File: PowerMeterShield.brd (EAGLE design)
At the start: 71.1 x 53.3 mm, 28 parts, among them IC1 MCP3426A0-E/SN, IC2 ISL21080, IC3 ADUM1250ARZ, U1 INA170EA/2K5, U2 THS4521

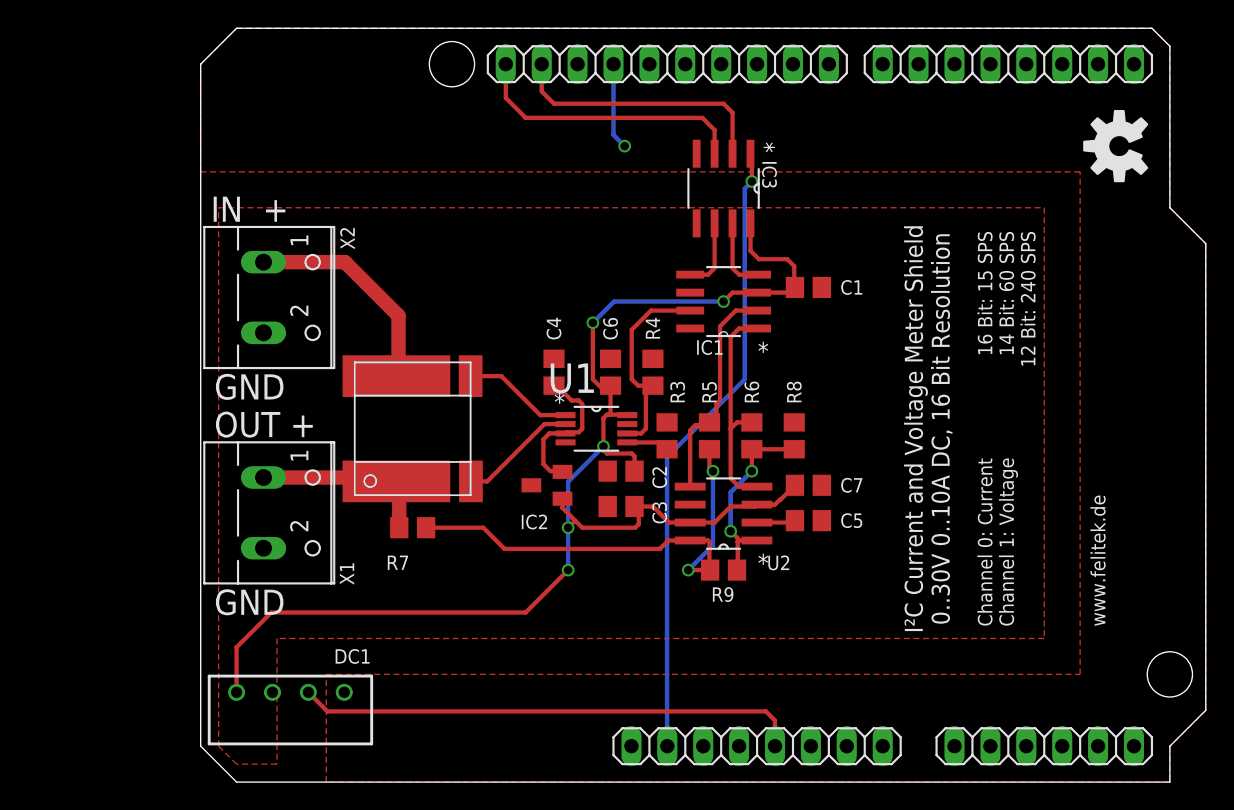
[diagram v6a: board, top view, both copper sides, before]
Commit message: Added non-isolated variant
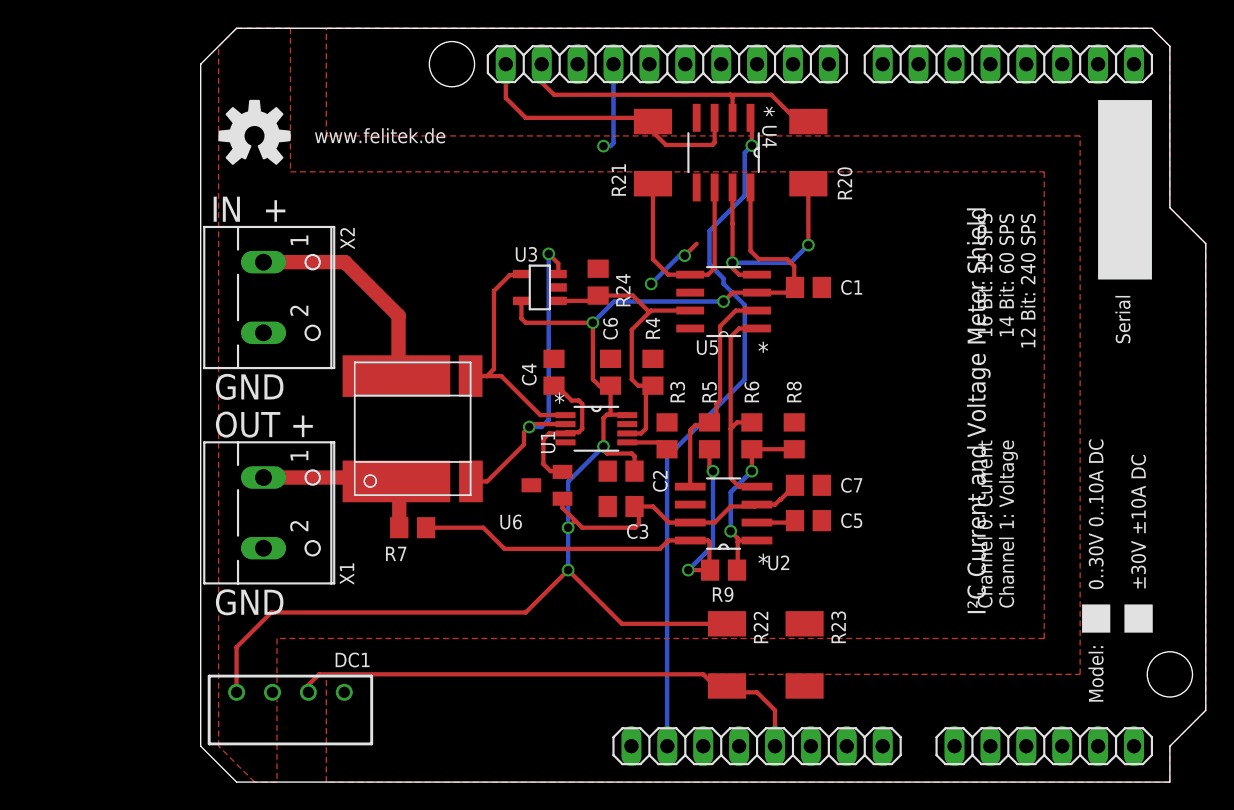
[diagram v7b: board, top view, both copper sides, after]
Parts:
- removed IC3: ADUM1250ARZ, Adum1250:SOIC127P600X175-8N
- added R20, R21, R22, R23: 0, rcl:R2010
- added R24: 20k, rcl:R0805
- added U3: INA138, burr-brown:SOT23-5
- added U4: ADUM1250ARZ, Adum1250:SOIC127P600X175-8N
- moved U$1 61.2 mm to (3.81, 45.7), turned to 0 degrees
- renumbered IC1 to U5, IC2 to U6, RS1 to R1
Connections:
- net +5V: now also R22.2
- net +5V/2: now also R22.1, U3.5, U4.8; no longer IC3.8
- net ADC2: now also R24.2, U3.1
- net CURRENT+: now also U3.3
- net CURRENT-: now also U3.4
- net GND: now also R23.2, U4.4; no longer IC3.4
- net GNDI: now also R23.1, R24.1, U3.2, U4.5; no longer IC3.5
- net IOREF: now also U4.1; no longer IC3.1
- net SCL: now also R21.2, U4.3; no longer IC3.3
- net SCLI: now also R21.1, U4.6; no longer IC3.6
- net SDA: now also R20.2, U4.2; no longer IC3.2
- net SDAI: now also R20.1, U4.7; no longer IC3.7
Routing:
- net +5V/2: track 97.9 -> 119.7 mm
- net CURRENT+: track 8.37 -> 23.9 mm, vias 0 -> 2
- net SDAI: track 5.09 -> 17.9 mm, vias 0 -> 2
- net SCLI: track 5.09 -> 16.1 mm
- net CURRENT-: track 7.86 -> 16.5 mm
- net ADC2: track 14.6 -> 21.7 mm
- net SDA: track 19.0 -> 24.1 mm
- net IOREF: track 44.5 -> 49.1 mm
- net GNDI: track 0.00 -> 4.56 mm, vias 0 -> 2
- net +5V: track 35.7 -> 38.1 mm
- net SCL: track 19.8 -> 21.1 mm
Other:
- board text added: "0..30V 0..10A DC"
- board text added: "I²C Current and Voltage Meter Shield"
- board text added: "Model:"
- board text added: "Serial"
- board text added: "±30V ±10A DC"
- board text removed: "I²C Current and Voltage Meter Shield 0..30V 0..10A DC, 16 Bit Resolution"

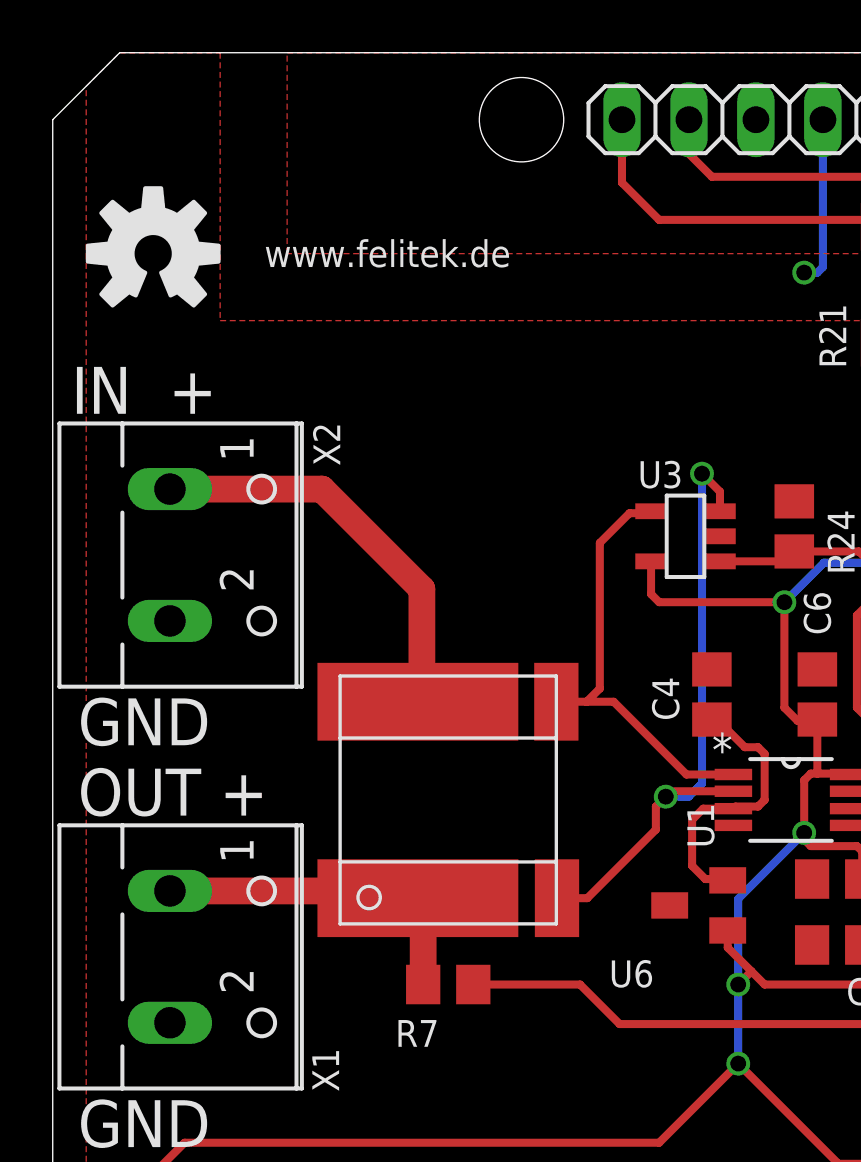
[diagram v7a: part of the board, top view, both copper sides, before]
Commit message: Moved logo and website a bit towards the top to align nicely with the isolation
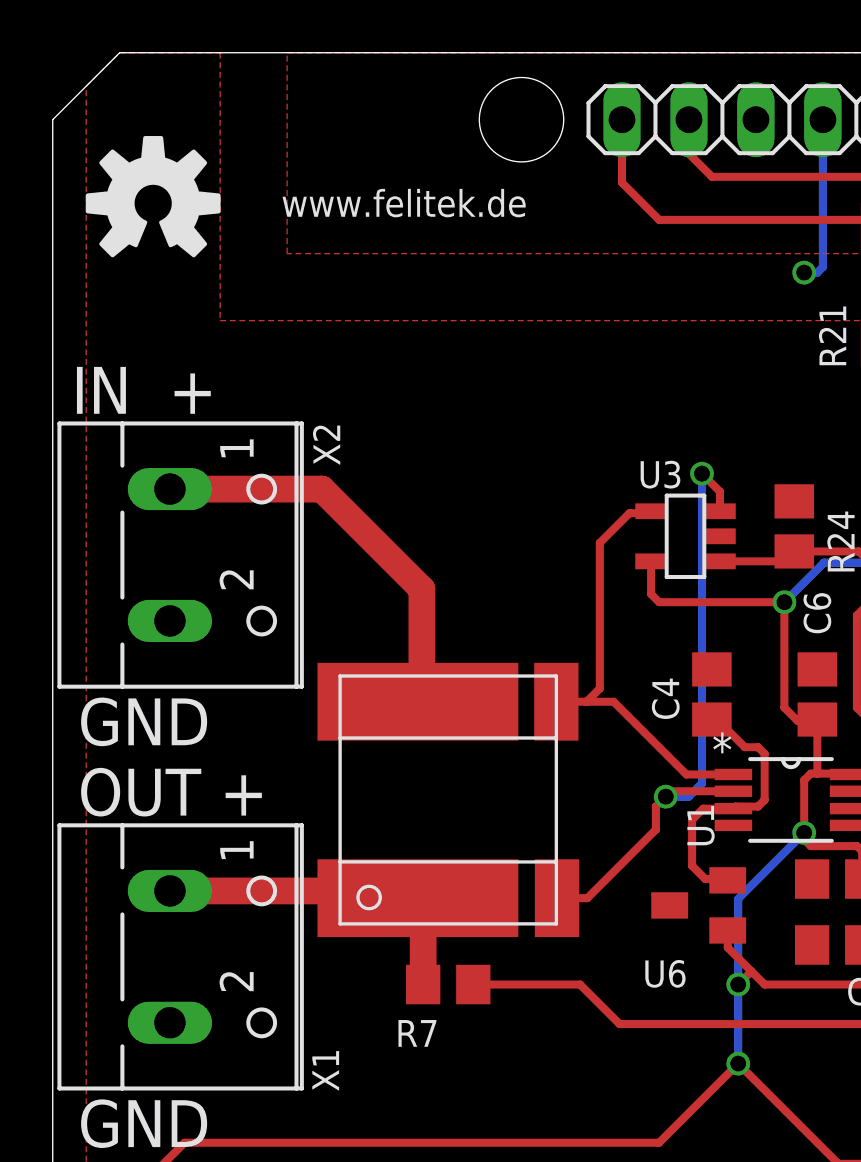
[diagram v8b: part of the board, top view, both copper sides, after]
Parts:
- moved U$1 1.91 mm to (3.81, 47.6)
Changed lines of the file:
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@@
 <rectangle x1="62.365" y1="10.57" x2="64.365" y2="12.57" layer="25"/>
 <rectangle x1="65.365" y1="10.57" x2="67.365" y2="12.57" layer="25"/>
-<text x="12.7" y="45.72" size="1.016" layer="25" align="center">www.felitek.de</text>
+<text x="13.335" y="47.625" size="1.016" layer="25" align="center">www.felitek.de</text>
 <rectangle x1="63.5" y1="35.56" x2="67.31" y2="48.26" layer="25"/>
 <text x="65.27" y="30.97" size="1.016" layer="25" rot="R90" align="center-left">Serial</text>
@@
 <attribute name="MF" value="MAXIM" x="24.5" y="21" size="1.778" layer="27" rot="R90" display="off"/>
 <attribute name="OC_FARNELL" value="unknown" x="24.5" y="21" size="1.778" layer="27" rot="R90" display="off"/>
-<attribute name="NAME" x="21.095" y="18.405" size="1.016" layer="25" align="center-left"/>
+<attribute name="NAME" x="22.365" y="18.405" size="1.016" layer="25" align="center-left"/>
 </element>
 <element name="R3" library="rcl" package="R0805" value="20k" x="33" y="24.5" smashed="yes" rot="R270">
@@
 <attribute name="NAME" x="45.25" y="21" size="1.016" layer="25" align="center-left"/>
 </element>
-<element name="U$1" library="SparkFun" package="OSHW-LOGO-M" value="" x="3.81" y="45.72"/>
+<element name="U$1" library="SparkFun" package="OSHW-LOGO-M" value="" x="3.81" y="47.625"/>
 <element name="R20" library="rcl" package="R2010" value="0" x="43" y="44.54" smashed="yes" rot="R90">
 <attribute name="NAME" x="46.095" y="41.115" size="1.016" layer="25" rot="R90"/>
@@
 <wire x1="25.306" y1="35.95" x2="25.306" y2="36.694" width="0.3048" layer="1"/>
 <wire x1="25.306" y1="36.694" x2="24.625" y2="37.375" width="0.3048" layer="1"/>
-<via x="24.625" y="37.375" extent="1-16" drill="0.6" shape="square"/>
+<via x="24.625" y="37.375" extent="1-16" drill="0.6"/>
 <wire x1="24.625" y1="37.375" x2="24.625" y2="25.625" width="0.3048" layer="16"/>
 <wire x1="20.275" y1="21.275" x2="22.875" y2="23.875" width="0.3048" layer="1"/>
